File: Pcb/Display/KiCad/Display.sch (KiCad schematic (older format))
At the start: 31 parts, among them J2 47219-2001, Q1 310mA/60V/1.6Ω

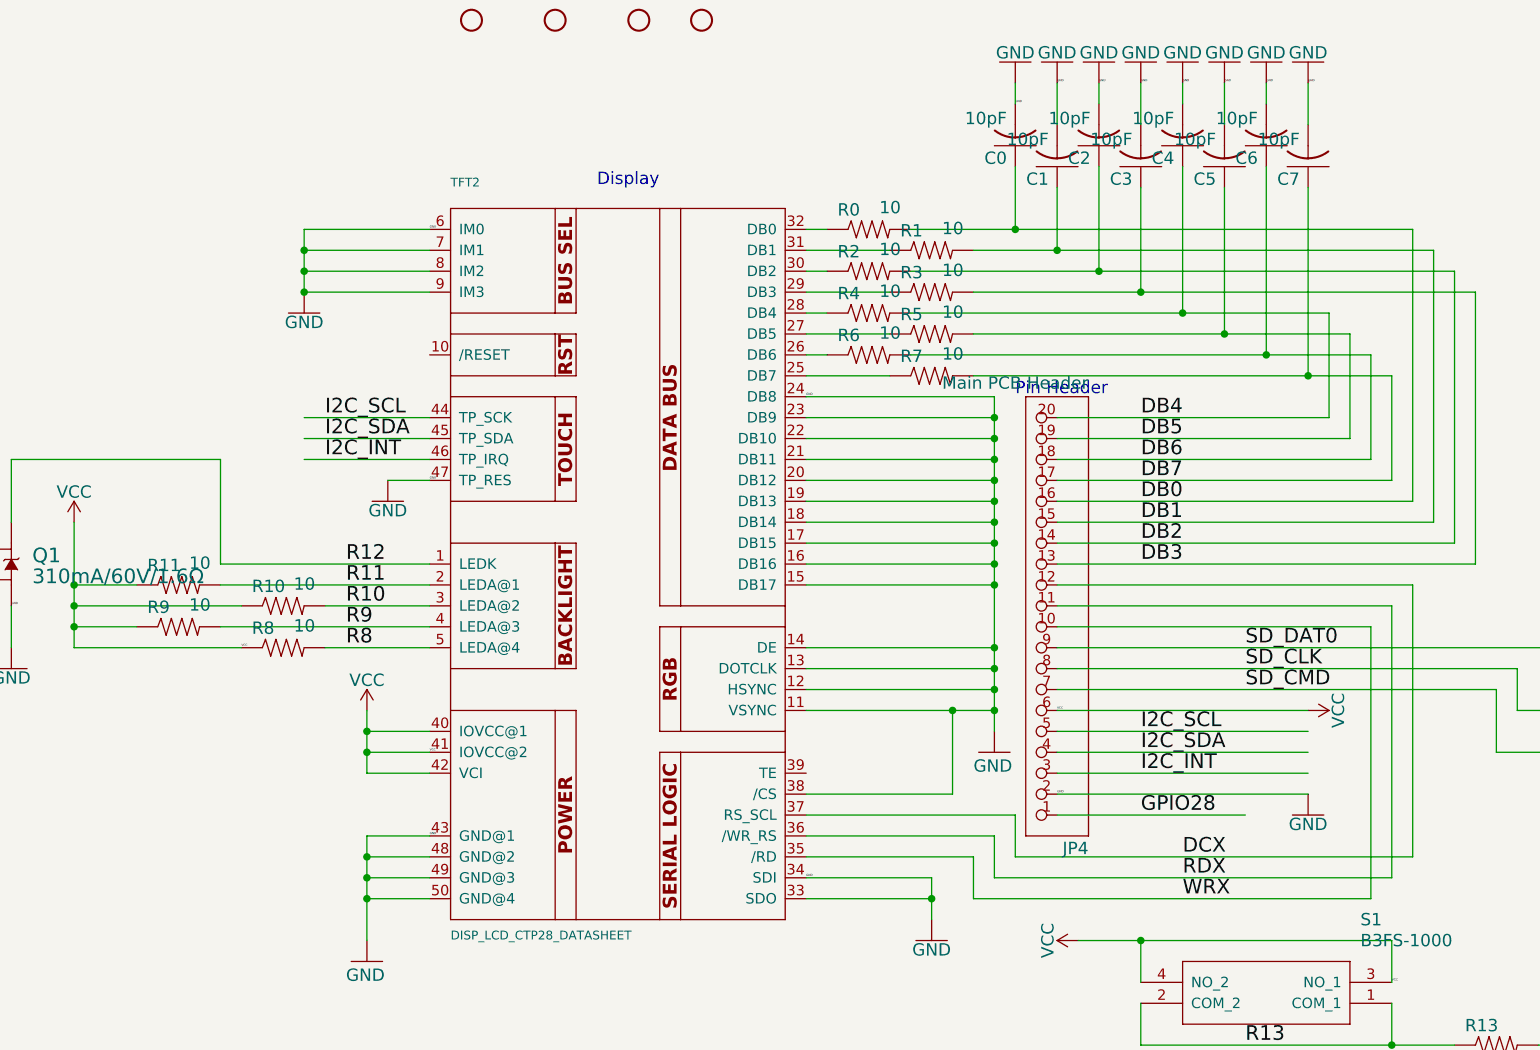
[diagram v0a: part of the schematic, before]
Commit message: Updated PCB files and ported some of the graphics functions. The graphics changes are not tested yet.
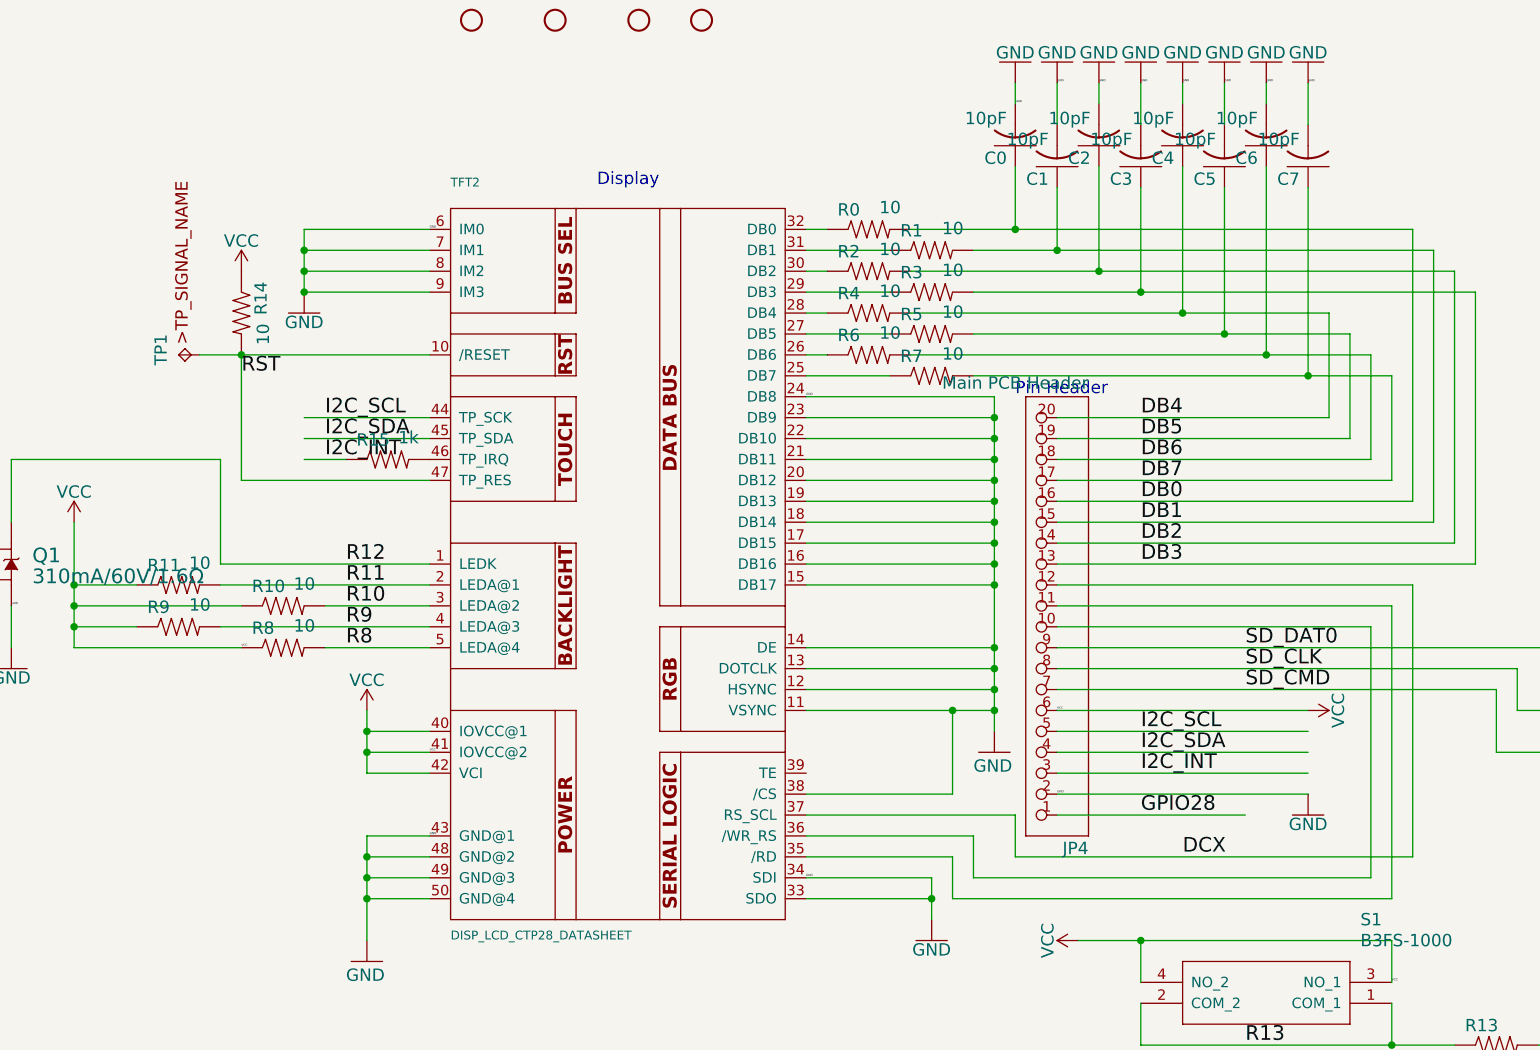
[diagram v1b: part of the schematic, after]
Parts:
- added R14: 10, Display:R0805, symbol Display-eagle-import:R-US_R0805
- added R15: 1k, Display:R0805, symbol Display-eagle-import:R-US_R0805
- added TP1: TPTP09R, Display:TP09R, symbol Display-eagle-import:TPTP09R
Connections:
- net labels added: RST
- net labels removed: RDX, WRX
- wire segments 185 -> 188
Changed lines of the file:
@@
 EESchema Schematic File Version 4
-EELAYER 29 0
+EELAYER 30 0
 EELAYER END
 $Descr User 16834 9698
@@
 GND
 Wire Wire Line
-	6100 3000 5900 3000
-Text Label 6100 3000 0    10   ~ 0
-GND
-Wire Wire Line
 	7900 4900 8500 4900
 Wire Wire Line
@@
 I2C_SDA
 Wire Wire Line
-	6100 2900 5500 2900
-Text Label 5600 2900 0    70   ~ 0
-I2C_INT
-Wire Wire Line
 	9100 4400 10300 4400
 Text Label 9500 4400 0    70   ~ 0
+I2C_INT
+Wire Wire Line
+	5700 2900 5500 2900
+Text Label 5600 2900 0    70   ~ 0
 I2C_INT
 Wire Wire Line
@@
 DCX
 Wire Wire Line
-	7900 4700 8800 4700
-Wire Wire Line
-	8800 4700 8800 4900
-Wire Wire Line
 	9100 3600 10700 3600
 Wire Wire Line
-	10700 3600 10700 4900
-Wire Wire Line
-	8800 4900 10700 4900
-Text Label 9700 4900 0    70   ~ 0
-RDX
-Wire Wire Line
-	7900 4800 8700 4800
-Wire Wire Line
-	8700 4800 8700 5000
+	10700 3600 10700 5000
+Wire Wire Line
+	8600 5000 10700 5000
+Wire Wire Line
+	8600 5000 8600 4800
+Wire Wire Line
+	8600 4800 7900 4800
+Wire Wire Line
+	8700 4700 8700 4900
 Wire Wire Line
 	9100 3700 10600 3700
 Wire Wire Line
-	10600 3700 10600 5000
-Wire Wire Line
-	8700 5000 10600 5000
-Text Label 9700 5000 0    70   ~ 0
-WRX
+	10600 3700 10600 4900
+Wire Wire Line
+	8700 4900 10600 4900
+Wire Wire Line
+	8700 4700 7900 4700
 Wire Wire Line
 	9500 5500 9500 5700
@@
 Wire Wire Line
 	8000 2400 7900 2400
+Wire Wire Line
+	6100 2400 5200 2400
+Wire Wire Line
+	5200 2400 5000 2400
+Wire Wire Line
+	5200 2400 5200 3000
+Wire Wire Line
+	5200 3000 6100 3000
+Connection ~ 5200 2400
+Text Label 5200 2500 0    70   ~ 0
+RST
 $Comp
 L Display-eagle-import:A3L-LOC #FRAME1
@@
 $EndComp
 $Comp
-L Display-eagle-import:GND #GND040
-U 1 1 2B74A96F
-P 5900 3100
-F 0 "#GND040" H 5900 3100 50  0001 C CNN
-F 1 "GND" H 5900 3090 59  0000 C TNN
-F 2 "" H 5900 3100 50  0001 C CNN
-F 3 "" H 5900 3100 50  0001 C CNN
-	1    5900 3100
-	1    0    0    -1
-$EndComp
-$Comp
 L Display-eagle-import:GND #GND041
 U 1 1 057C4BD5
@@
 	1    0    0    -1
 $EndComp
+$Comp
+L Display-eagle-import:R-US_R0805 R14
+U 1 1 2C7B912C
+P 5200 2200
+F 0 "R14" H 5050 2259 59  0000 L BNN
+F 1 "10" H 5250 2270 59  0000 L BNN
+F 2 "Display:R0805" H 5200 2200 50  0001 C CNN
+F 3 "" H 5200 2200 50  0001 C CNN
+	1    5200 2200
+	0    1    1    0
+$EndComp
+$Comp
+L Display-eagle-import:VCC #SUPPLY03
+U 1 1 4F8E092B
+P 5200 2000
+F 0 "#SUPPLY03" H 5200 2000 50  0001 C CNN
+F 1 "VCC" H 5200 2110 59  0000 C BNN
+F 2 "" H 5200 2000 50  0001 C CNN
+F 3 "" H 5200 2000 50  0001 C CNN
+	1    5200 2000
+	1    0    0    -1
+$EndComp
+$Comp
+L Display-eagle-import:TPTP09R TP1
+U 1 1 FE5B29FD
+P 4900 2400
+F 0 "TP1" H 4850 2450 59  0000 L BNN
+F 1 "TPTP09R" H 4900 2400 50  0001 C CNN
+F 2 "Display:TP09R" H 4900 2400 50  0001 C CNN
+F 3 "" H 4900 2400 50  0001 C CNN
+	1    4900 2400
+	0    -1   -1   0
+$EndComp
+$Comp
+L Display-eagle-import:R-US_R0805 R15
+U 1 1 6F379528
+P 5900 2900
+F 0 "R15" H 5750 2959 59  0000 L BNN
+F 1 "1k" H 5950 2970 59  0000 L BNN
+F 2 "Display:R0805" H 5900 2900 50  0001 C CNN
+F 3 "" H 5900 2900 50  0001 C CNN
+	1    5900 2900
+	1    0    0    -1
+$EndComp
